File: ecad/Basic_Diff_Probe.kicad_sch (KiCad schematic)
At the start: 28 parts, among them J1 9V Battery Input, J2 To Scope, J3 Differential Input, SW1 SW_SPDT, SW2 SW_SPST, U1 LM6321N, U2 LMC6484AIN

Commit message: schematic
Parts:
- removed C2: C, symbol Device:C
- removed J3: Differential Input, symbol Connector:Screw_Terminal_01x02
- removed R3: 10k, symbol Device:R_US
- removed SW1: SW_SPDT, symbol Switch:SW_SPDT
- removed SW2: SW_SPST, symbol Switch:SW_SPST
- removed U1: LM6321N, Package_DIP:DIP-8_W7.62mm, symbol Amplifier_Buffer:LM6321N
- added C5: 10pF, Capacitor_THT:C_Disc_D6.0mm_W2.5mm_P5.00mm, symbol Device:C
- added D4: 1N5817, Diode_THT:D_DO-41_SOD81_P10.16mm_Horizontal, symbol Diode:1N5817
- added H1, H2, H3, H4: M3, MountingHole:MountingHole_3.2mm_M3, symbol Mechanical:MountingHole
- added J3: Differential Input, symbol Connector:Conn_Coaxial
- added R16: 100k, Resistor_THT:R_Axial_DIN0207_L6.3mm_D2.5mm_P7.62mm_Horizontal, symbol Device:R_US
- added SW1: EG2209A, symbol Switch:SW_Push_DPDT
- added TP1, TP2, TP3, TP4, TP5, TP6: TestPoint, TestPoint:TestPoint_Keystone_5000-5004_Miniature, symbol Connector:TestPoint
- C1, C3, C4: footprint (none) -> Capacitor_THT:C_Disc_D6.0mm_W2.5mm_P5.00mm
- D1: value LED -> WP7113ID; footprint (none) -> LED_THT:LED_D5.0mm
- D2: value D_Zener -> SA10A; footprint (none) -> Diode_THT:D_DO-15_P10.16mm_Horizontal
- D3: value D_TVS -> SA9.0CA; footprint (none) -> Diode_THT:D_DO-15_P10.16mm_Horizontal
- F1: footprint (none) -> Fuse:Fuse_1206_3216Metric_Pad1.42x1.75mm_HandSolder
- J1: footprint (none) -> TerminalBlock_Phoenix:TerminalBlock_Phoenix_MKDS-1,5-2-5.08_1x02_P5.08mm_Horizontal
- R1: value R_US -> 1.4k; footprint (none) -> Resistor_THT:R_Axial_DIN0207_L6.3mm_D2.5mm_P7.62mm_Horizontal
- R10, R11, R9: footprint (none) -> Resistor_THT:R_Axial_DIN0207_L6.3mm_D2.5mm_P7.62mm_Horizontal
- R12, R13: value R_US -> 900k; footprint (none) -> Resistor_THT:R_Axial_DIN0207_L6.3mm_D2.5mm_P7.62mm_Horizontal
- R2: value 10k -> 0; footprint (none) -> Resistor_THT:R_Axial_DIN0207_L6.3mm_D2.5mm_P7.62mm_Horizontal
- R4, R5, R6, R7: value R_US -> 10k; footprint (none) -> Resistor_THT:R_Axial_DIN0207_L6.3mm_D2.5mm_P7.62mm_Horizontal
- R8: value R_US -> 100; footprint (none) -> Resistor_THT:R_Axial_DIN0207_L6.3mm_D2.5mm_P7.62mm_Horizontal
- U2: footprint (none) -> Package_DIP:DIP-14_W7.62mm
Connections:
- net GND: now also R2.2, R9.2, U2.9 (-), R16.1, TP2.1; no longer C1.2, C3.2, D1.1 (K), D2.2 (A), D3.1 (A1), J1.1 (Pin_1), R11.2, U2.11 (V-), U2.12 (+)
- net at R4.2, R8.1, U2.7: now also C5.2
- net at J2.1 (In), R8.2: now also TP4.1
- net at D3.2 (A2), R12.2, R9.1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: now also SW1.3 (C), TP1.1
- net at C3.1: now also R10.2, R11.1, U2.10 (+); no longer R2.2
- net at R13.1: now also D3.1 (A1), U2.12 (+), R16.2, SW1.4 (A), TP3.1
- net at J1.2 (Pin_2): now also D4.2 (A); no longer F1.1
- net at R12.1: now also SW1.1 (A); no longer R13.2
- net at R4.1, R7.2, U2.6 (-): now also C5.1
- net at U2.8: now also R2.1; no longer U2.9 (-)
- net +9V renamed +BATT
- net +BATT: now also TP5.1; no longer R2.1
- new net: J3.1 (In), SW1.2 (B)
- new net: J3.2 (Ext), SW1.5 (B)
- new net: R13.2, SW1.6 (C)
- new net: D4.1 (K), F1.1
- new net -BATT: C1.2, C3.2, D1.1 (K), D2.2 (A), J1.1 (Pin_1), R11.2, TP6.1, U2.11 (V-)
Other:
- moved on the sheet: C1, C3, C4, D1, D2, D3, F1, J1, J2, R1, R10, R11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

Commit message: outputs
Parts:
- removed H1, H2, H3, H4: M3, MountingHole:MountingHole_3.2mm_M3, symbol Mechanical:MountingHole
- added C2: 0.1uF, Capacitor_THT:C_Disc_D6.0mm_W2.5mm_P5.00mm, symbol Device:C
- added H1, H2, H3, H4: M3, MountingHole:MountingHole_3.2mm_M3_Pad_Via, symbol Mechanical:MountingHole_Pad
- added J4: GND Output, TerminalBlock_Phoenix:TerminalBlock_Phoenix_MKDS-1,5-2-5.08_1x02_P5.08mm_Horizontal, symbol Connector:Screw_Terminal_01x02
- F1: value 100mA -> 125mA
- J2, J3: footprint (none) -> Connector_Coaxial:BNC_Amphenol_031-5539_Vertical
- R12, R13: value 900k -> 900k+/-0.1%
- R16, R9: value 100k -> 100k+/-0.1%
- R4, R5, R6, R7: value 10k -> 10k+/-0.1%
- SW1: footprint (none) -> Diff_Probe_Parts:SW_EG2209A
- TP1, TP2, TP3, TP4, TP5: value TestPoint -> 4952; footprint TestPoint:TestPoint_Keystone_5000-5004_Miniature -> TestPoint:TestPoint_THTPad_2.5x2.5mm_Drill1.2mm
- TP6: footprint TestPoint:TestPoint_Keystone_5000-5004_Miniature -> TestPoint:TestPoint_THTPad_2.5x2.5mm_Drill1.2mm
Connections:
- net +BATT: now also C4.2; no longer C4.1
- net -BATT: now also C2.2
- net GND: now also C4.1, C2.1, H1.1, H2.1, H3.1, H4.1, J4.1 (Pin_1), J4.2 (Pin_2); no longer C4.2
- net at D3.1 (A1), R13.1, R16.2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: now also SW1.6 (C); no longer SW1.4 (A)
- net at R13.2: now also SW1.4 (A); no longer SW1.6 (C)
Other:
- moved on the sheet: C1, C3, C4, C5, D1, D2, D3, D4, F1, J1, J2, J3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

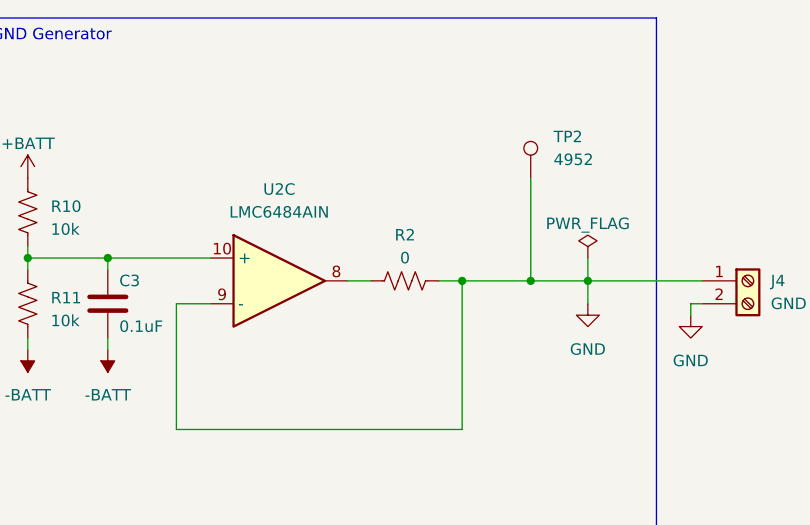
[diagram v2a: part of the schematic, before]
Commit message: chage 0 to 680
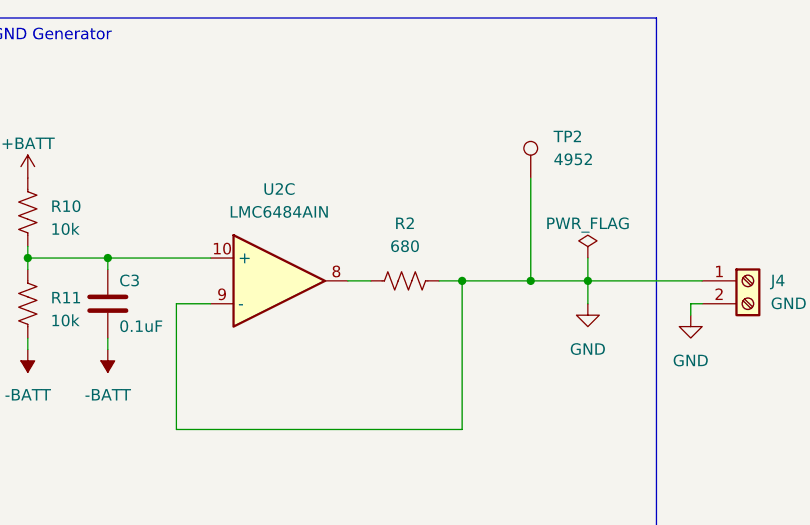
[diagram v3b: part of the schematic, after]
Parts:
- R2: value 0 -> 680
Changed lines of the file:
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@@
   (symbol (lib_id "Device:R_US") (at 177.8 45.72 90) (unit 1)
     (in_bom yes) (on_board yes) (dnp no) (fields_autoplaced)
-    (property "Reference" "R2" (at 177.8 40.64 90)
+    (property "Reference" "R2" (at 177.8 39.37 90)
       (effects (font (size 1.27 1.27)))
     )
-    (property "Value" "0" (at 177.8 43.18 90)
+    (property "Value" "680" (at 177.8 41.91 90)
       (effects (font (size 1.27 1.27)))
     )
